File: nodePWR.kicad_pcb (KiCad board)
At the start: 2 copper layers, 0 parts

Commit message: Checkpoint - starting PCB
On branch master
modified:   nodePWR-cache.lib
modified:   nodePWR.kicad_pcb
modified:   nodePWR.pro
modified:   nodePWR.sch
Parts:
- added BT1: LiFeP04, rockingdlabs:JST_PH_S2B-PH-SM4-TB_02x2.00mm_Angled, F.Cu at (136.6, 85.8)
- added C1: 1 uF, Capacitors_SMD:C_0603, F.Cu at (129.4, 102.6)
- added C2: 2 uF, Capacitors_SMD:C_0603, F.Cu at (147.6, 97.6)
- added D1: Charging, LEDs:LED_0603, F.Cu at (149.2, 92.0)
- added P1: Vin (4.5-30VDC), Pin_Headers:Pin_Header_Straight_1x02, F.Cu at (148.2, 84.9)
- added P2: USB (power only), Connect:USB_Micro-B_10103594-0001LF, F.Cu at (138.6, 98.6)
- added P3: Node, rockingdlabs:FPC_conn-6_8x4.9mm_Pitch0.5mm, F.Cu at (121.2, 105.4)
- added P4: Serial I/O, Pin_Headers:Pin_Header_Angled_1x06, F.Cu at (120.7, 84.9)
- added R1: 10k, Resistors_SMD:R_0603, F.Cu at (165.9, 81.7)
- added R2: 1k, Resistors_SMD:R_0603, F.Cu at (151.2, 98.5)
- added R3: 75, Resistors_SMD:R_0603, F.Cu at (169.2, 81.7)
- added R4: 490k, Resistors_SMD:R_0603, F.Cu at (166.4, 87.7)
- added R5: 100k, Resistors_SMD:R_0603, F.Cu at (155.0, 98.5)
- added SW1: Prgm, Buttons_Switches_SMD:SW_SPDT_PCM12, F.Cu at (159.6, 83.0)
- added U1: bq25070, Housings_DFN_QFN:DFN-10-1EP_2x3mm_Pitch0.5mm, F.Cu at (158.5, 91.9)

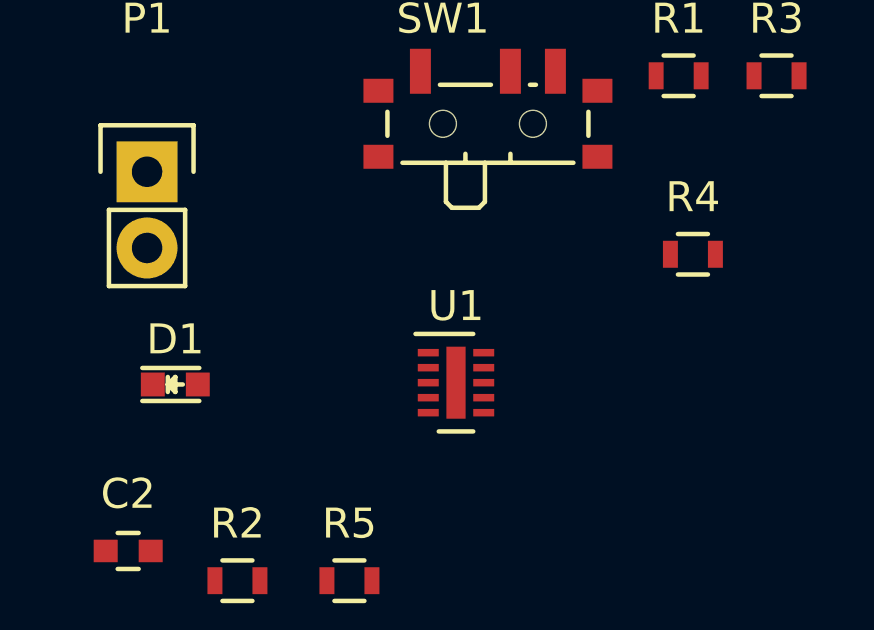
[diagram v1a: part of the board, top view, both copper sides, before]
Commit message: Use TI/Ultra-librarian footprint for bq25070
On branch master
modified:   nodePWR.kicad_pcb
modified:   nodePWR.sch
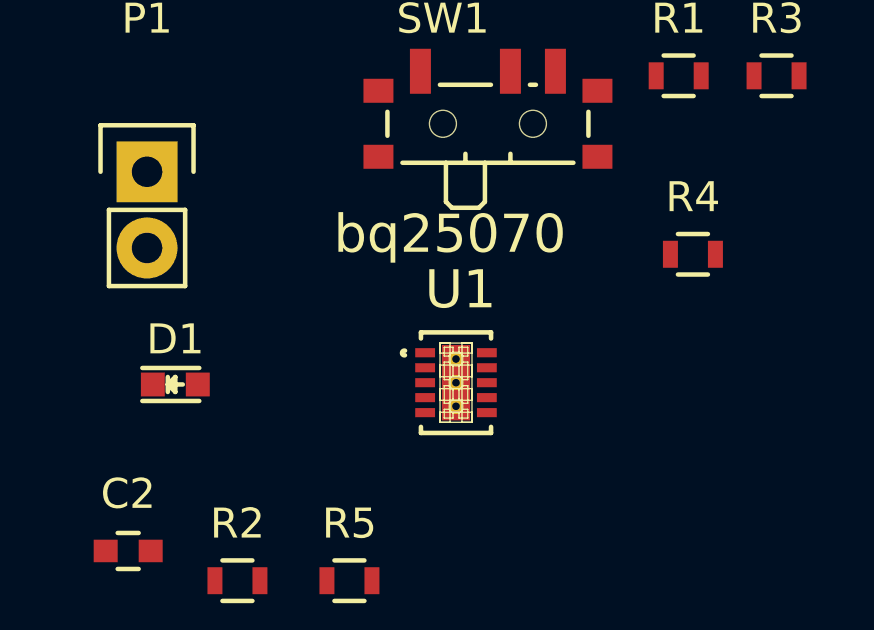
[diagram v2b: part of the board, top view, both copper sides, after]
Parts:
- U1: footprint Housings_DFN_QFN:DFN-10-1EP_2x3mm_Pitch0.5mm -> rockingdlabs:bq25070_DQC_10-DQC10_P84X2P4

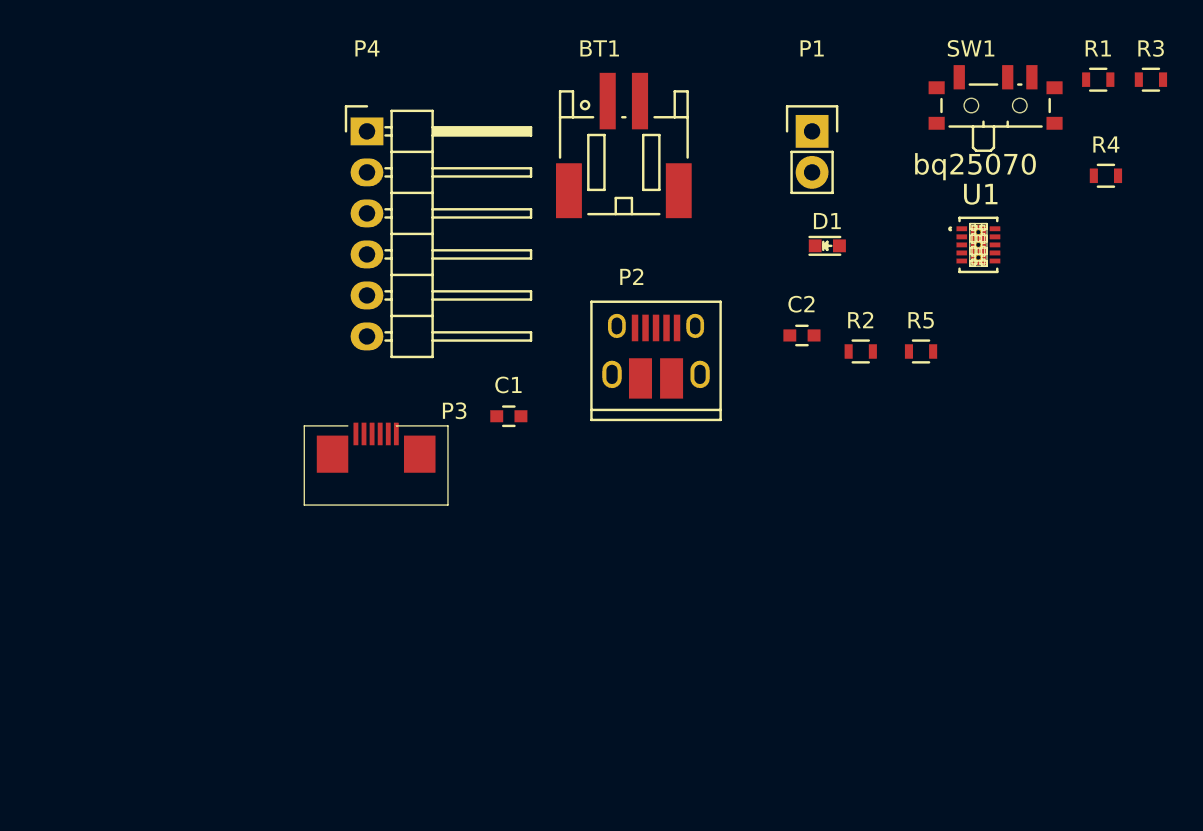
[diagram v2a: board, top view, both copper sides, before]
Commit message: Check-point: parts placed
    - board size 20.5mm high to match TLPNode

On branch master
modified:   nodePWR.kicad_pcb
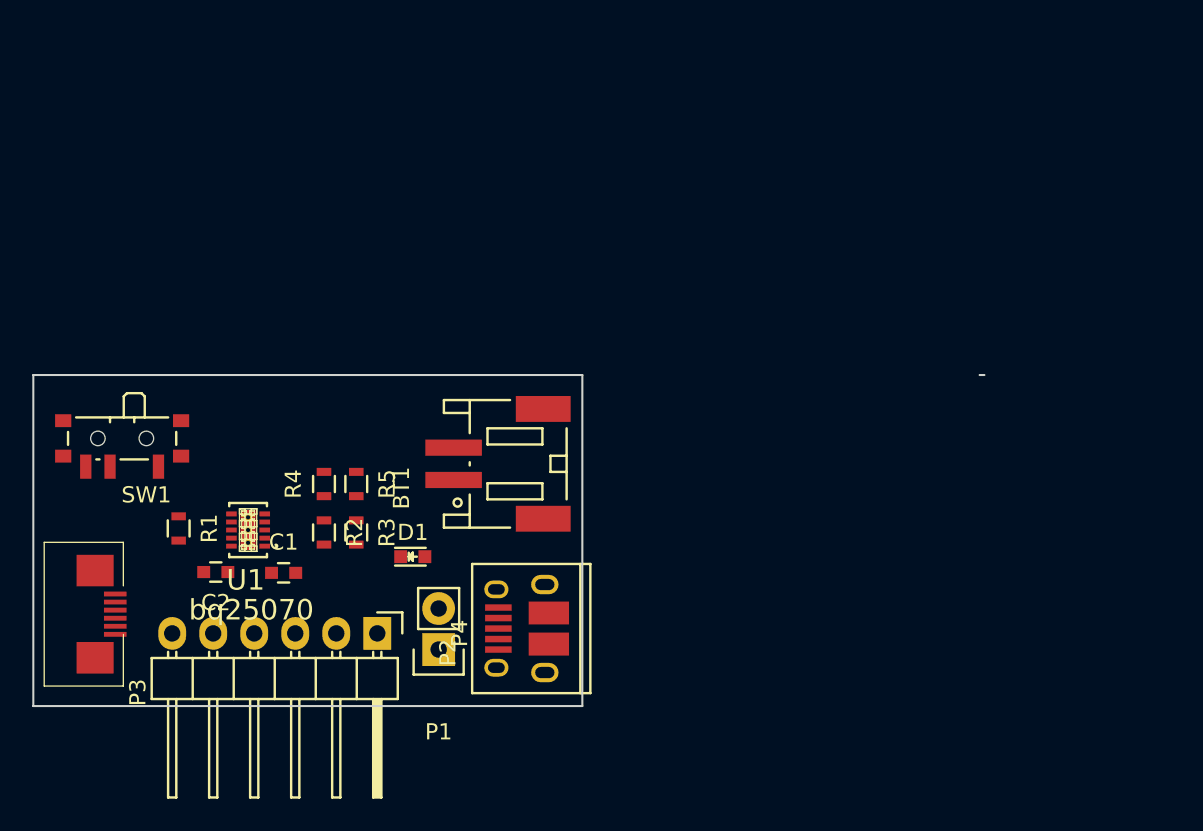
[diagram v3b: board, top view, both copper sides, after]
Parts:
- moved R1 63.4 mm to (109.0, 109.5), turned to 270 degrees
- moved SW1 58.1 mm to (105.5, 104.2), turned to 180 degrees
- moved R3 56.6 mm to (120.0, 109.8), turned to 270 degrees
- moved R4 52.0 mm to (118.0, 106.8), turned to 90 degrees
- moved U1 48.5 mm to (113.3, 109.6), turned to 180 degrees
- moved P1 39.6 mm to (125.1, 117.0), turned to 180 degrees
- moved C2 39.1 mm to (111.3, 112.2), turned to 180 degrees
- moved R5 35.9 mm to (120.0, 106.8), turned to 270 degrees
- moved R2 35.1 mm to (118.0, 109.8), turned to 270 degrees
- moved D1 32.1 mm to (123.5, 111.2)
- moved P4 31.1 mm to (121.3, 116.0), turned to 270 degrees
- moved BT1 21.2 mm to (128.8, 105.5), turned to 90 degrees
- moved P3 20.2 mm to (103.3, 114.8), turned to 270 degrees
- moved P2 19.0 mm to (130.3, 115.7), turned to 90 degrees
- moved C1 17.0 mm to (115.5, 112.2)
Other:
- board outline added: 58.9 x 20.5 mm
- net class Default: clearance 0.254 -> 0.1524; trace_width 0.254 -> 0.1524
- rule trace_clearance: 0.254 -> 0.1524
